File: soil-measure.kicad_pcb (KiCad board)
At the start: 4 copper layers, 90 x 40 mm, 132 parts, among them J1 JAE_SIM_Card_SF72S006, J2 Conn_Coaxial, J3 USB_B, J4 Conn_Coaxial, J5 USB_C_Receptacle_USB2.0_14P, J6 DE9_Socket_MountingHoles, J7 Conn_01x16, Q1 SS8050, Q2 SS8050, Q3 SS8050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

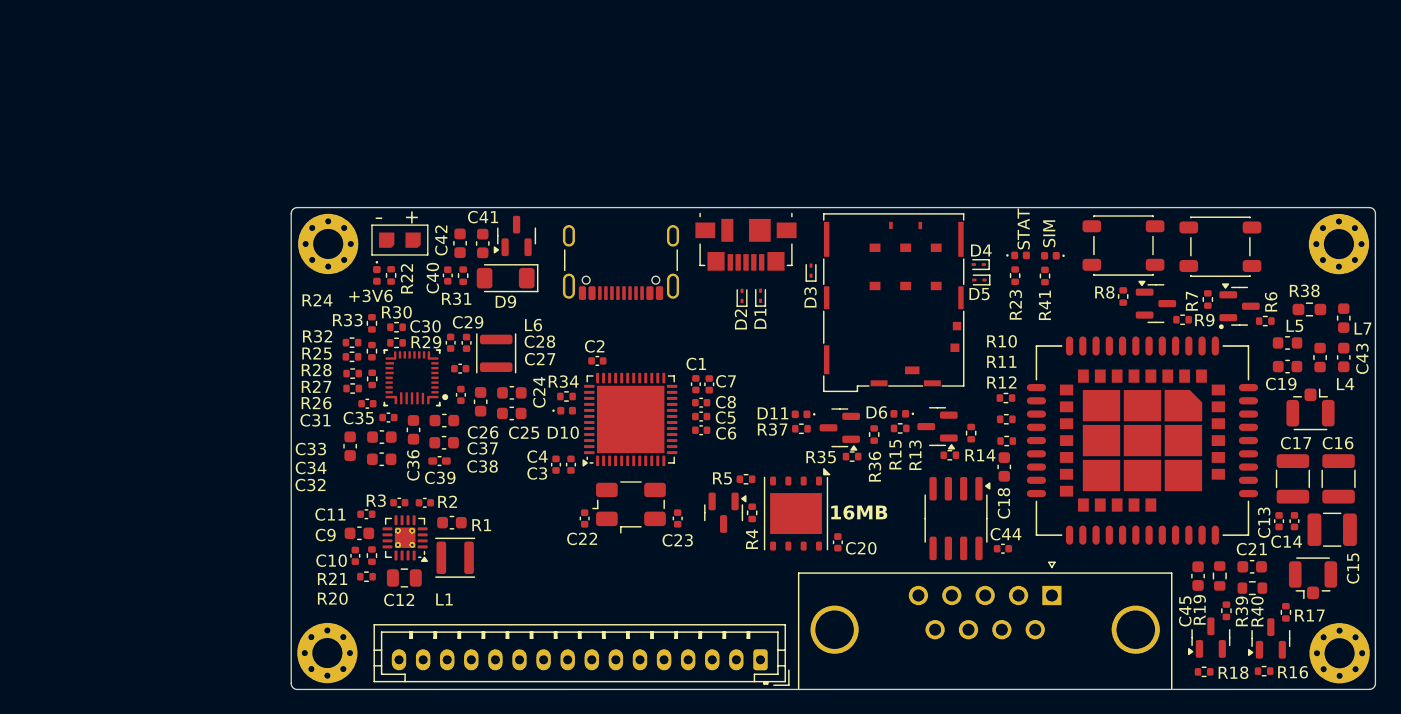
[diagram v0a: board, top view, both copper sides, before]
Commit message: Fixed bug on schematic
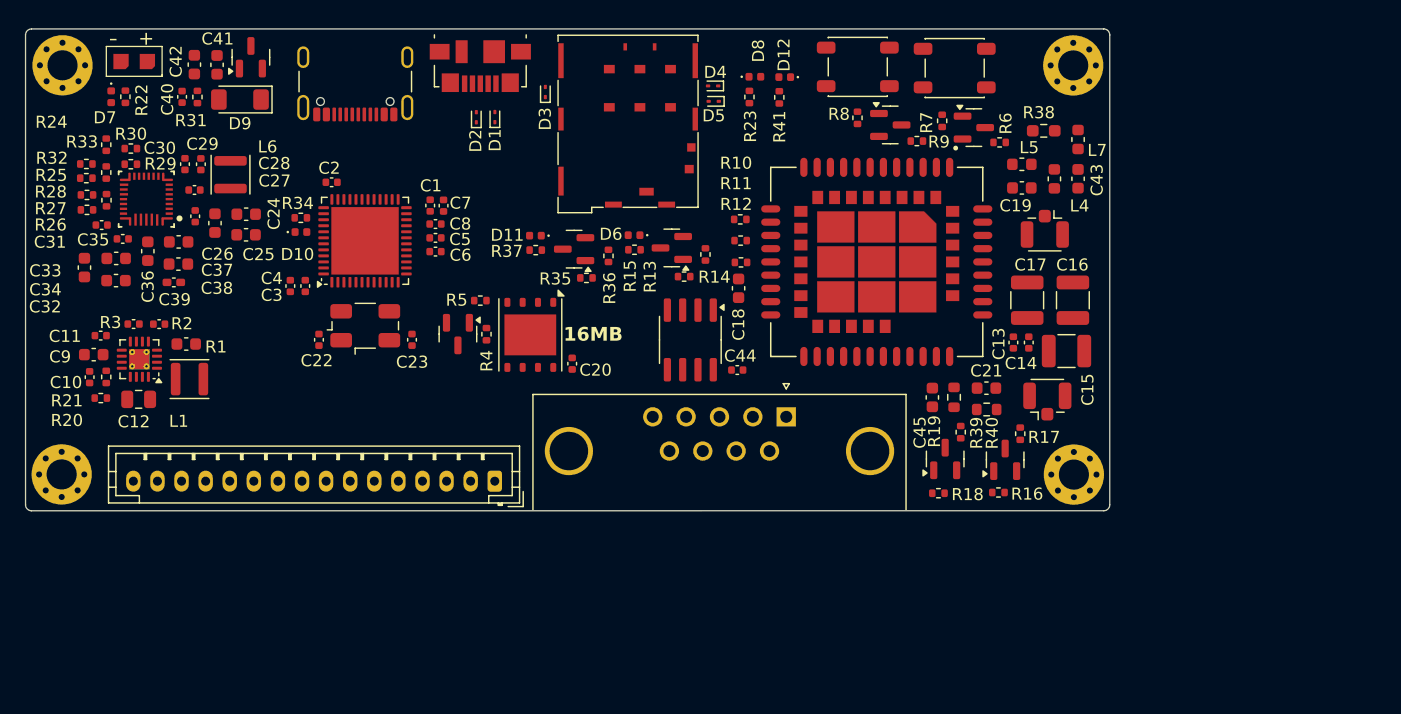
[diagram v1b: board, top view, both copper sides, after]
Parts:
- moved C16 26.6 mm to (173.8, 89.2)
- moved C17 26.6 mm to (170.0, 89.2)
- moved C38 26.6 mm to (99.6, 86.2)
- moved D11 26.6 mm to (129.2, 83.8)
- moved D7 26.6 mm to (94.0, 72.3)
- moved L1 26.6 mm to (100.5, 95.8)
- moved R12 26.6 mm to (146.3, 86.1)
- moved R2 26.6 mm to (98.0, 91.2)
- moved R38 26.6 mm to (171.4, 75.1)
- moved U5 26.6 mm to (96.9, 80.8)
- moved C12 26.6 mm to (96.3, 97.4)
- moved C15 26.6 mm to (173.3, 93.4)
- moved C18 26.6 mm to (146.1, 88.2)
- moved C19 26.6 mm to (169.6, 79.9)
- moved C2 26.6 mm to (112.3, 79.4)
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- renumbered SIM to D12, +3V6 to D7, STAT to D8
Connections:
- net Net-(D1-A2) renamed /cellular_interface/DN
- net Net-(D2-A2) renamed /cellular_interface/DP
- J5 pad A6: /MCU_DM -> /MCU_DP
- J5 pad A7: /MCU_DP -> /MCU_DN
- J5 pad B6: /MCU_DM -> /MCU_DP
- J5 pad B7: /MCU_DP -> /MCU_DN
- U1 pad 33: /MCU_DM -> /MCU_DN

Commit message: changed footprint for component BQ25672RQMR and routed a controlled impedance trace over the USB interfaces, at 90ohm DI
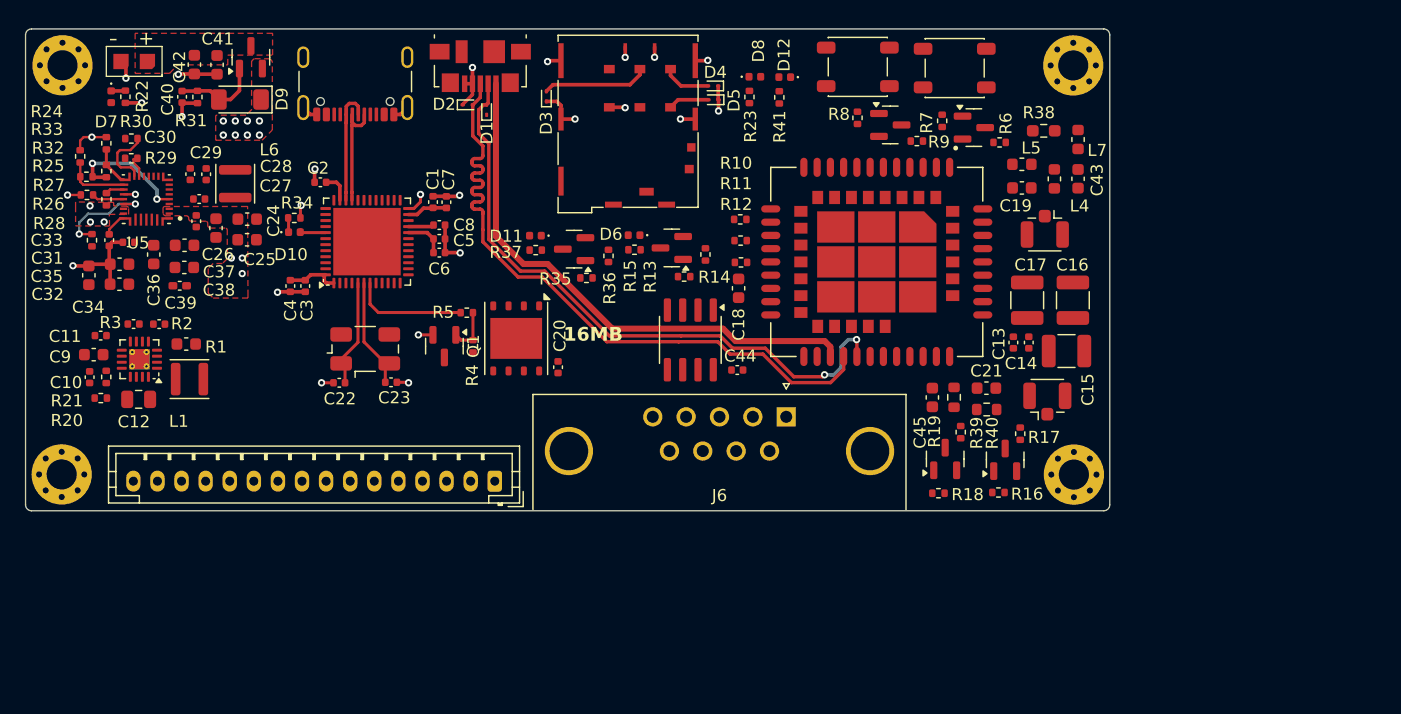
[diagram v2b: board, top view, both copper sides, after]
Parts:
- U5: footprint BQ25672:RQM0029A-MFG -> BQ25672:IC_BQ25672RQMR
- moved C22 3.94 mm to (112.9, 96.1), turned to 180 degrees
- moved C23 3.93 mm to (117.2, 96.0), turned to 0 degrees
- moved R28 2.55 mm to (92.4, 84.2), turned to 90 degrees
- moved Y1 1.92 mm to (115.1, 93.3)
- moved R5 1.50 mm to (123.5, 90.2)
- moved R4 1.50 mm to (124.0, 93.0)
- moved Q1 1.50 mm to (121.6, 93.0)
- moved C31 1.40 mm to (93.8, 84.2), turned to 90 degrees
- moved D2 1.25 mm to (123.6, 73.0), turned to 0 degrees
- moved C20 1.21 mm to (131.1, 94.8)
- moved U4 1.21 mm to (127.6, 92.4)
- moved C29 0.94 mm to (101.9, 78.8)
- moved C30 0.94 mm to (100.5, 78.7)
- moved C2 0.94 mm to (111.3, 79.4)
- moved D1 0.92 mm to (125.1, 73.4)
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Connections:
- net Net-(Q7-D) renamed /battery_charger/VIN_P
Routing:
- net /cellular_interface/DP: track 0.00 -> 55.6 mm
- net GND: track 0.00 -> 53.0 mm, vias 0 -> 24
- net /cellular_interface/DN: track 0.00 -> 52.7 mm, vias 0 -> 2
- net MOD_VBUS: track 0.00 -> 45.0 mm
- net +3V6: track 0.00 -> 15.9 mm
- net REGN: track 0.00 -> 10.3 mm, vias 0 -> 2
- net Net-(U1-PF1): track 0.00 -> 10.1 mm
- net /MCU_DN: track 0.00 -> 9.68 mm
- net /MCU_DP: track 0.00 -> 9.68 mm
- net /PWR_CTR: track 0.00 -> 9.57 mm
- net Net-(U1-PF0): track 0.00 -> 9.00 mm
- net Net-(D3-A2): track 0.00 -> 8.80 mm
- net CHG_INT: track 0.00 -> 8.30 mm, vias 0 -> 2
- net Net-(D9-A): track 0.00 -> 7.20 mm
- net /CHG_SDA: track 0.00 -> 5.40 mm
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- added copper zone on F.Cu, net /battery_charger/VIN_P
- added copper zone on F.Cu, net VBATP
- added copper zone on F.Cu, net VBUS
